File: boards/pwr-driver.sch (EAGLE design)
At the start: 24 parts

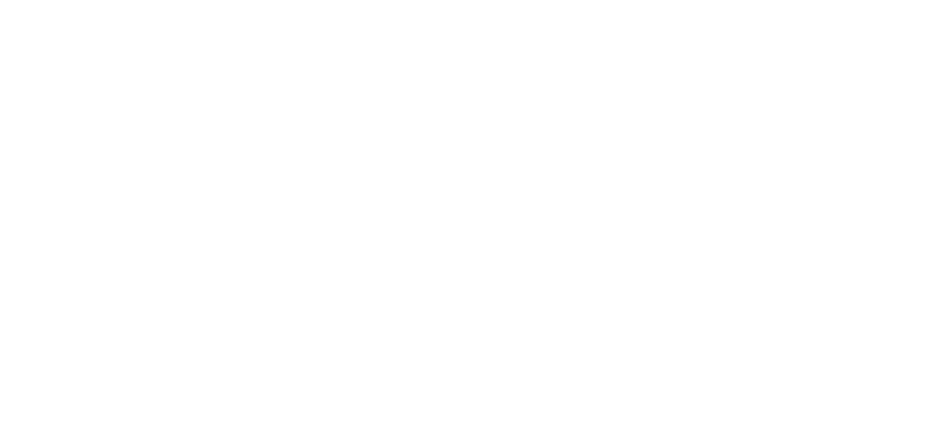
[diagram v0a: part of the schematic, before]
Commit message: dding start of parts lib for breakout board.
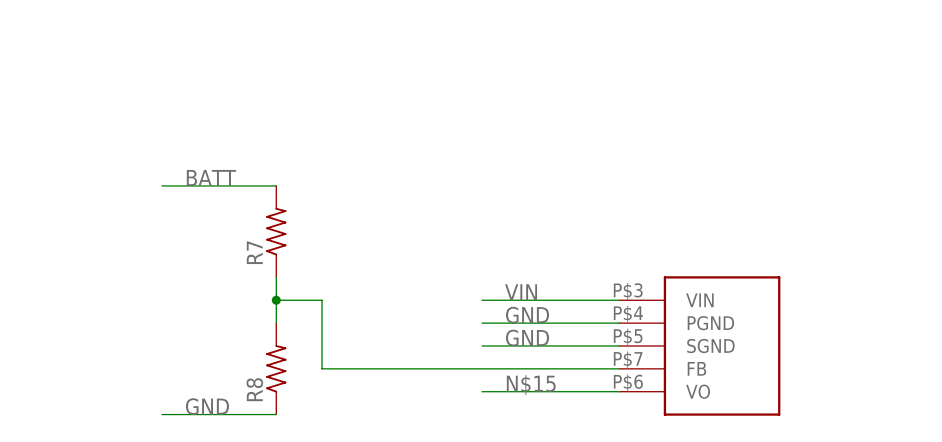
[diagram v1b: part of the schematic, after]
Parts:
- added R7, R8: (no value), resistor:R-US_R0603
- added U$1: MPM80, needed-parts:MPM80
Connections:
- new net BATT: R7.2
- new net N$15: U$1.VO
- new net N$4: R7.1, R8.2, U$1.FB
- net GND: now also R8.1, U$1.PGND, U$1.SGND
- net VIN: now also U$1.VIN
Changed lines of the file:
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@@
 <part name="R6" library="resistor" deviceset="R-US_" device="R0603" value="10k"/>
 <part name="C5" library="resistor" deviceset="C-US" device="C0603" value=".1uf"/>
+<part name="U$1" library="needed-parts" deviceset="MPM80" device=""/>
+<part name="R7" library="resistor" deviceset="R-US_" device="R0603"/>
+<part name="R8" library="resistor" deviceset="R-US_" device="R0603"/>
 </parts>
 <sheets>
@@
 <instance part="R6" gate="G$1" x="-66.04" y="20.32"/>
 <instance part="C5" gate="G$1" x="-68.58" y="15.24" rot="R90"/>
+<instance part="U$1" gate="G$1" x="96.52" y="-38.1"/>
+<instance part="R7" gate="G$1" x="48.26" y="-20.32" rot="R90"/>
+<instance part="R8" gate="G$1" x="48.26" y="-35.56" rot="R90"/>
 </instances>
 <busses>
@@
 <junction x="-71.12" y="15.24"/>
 </segment>
+<segment>
+<pinref part="R8" gate="G$1" pin="1"/>
+<wire x1="48.26" y1="-40.64" x2="35.56" y2="-40.64" width="0.1524" layer="91"/>
+<label x="38.1" y="-40.64" size="1.778" layer="95"/>
+</segment>
+<segment>
+<pinref part="U$1" gate="G$1" pin="PGND"/>
+<wire x1="86.36" y1="-30.48" x2="71.12" y2="-30.48" width="0.1524" layer="91"/>
+<label x="73.66" y="-30.48" size="1.778" layer="95"/>
+</segment>
+<segment>
+<pinref part="U$1" gate="G$1" pin="SGND"/>
+<wire x1="86.36" y1="-33.02" x2="71.12" y2="-33.02" width="0.1524" layer="91"/>
+<label x="73.66" y="-33.02" size="1.778" layer="95"/>
+</segment>
 </net>
 <net name="3V3" class="0">
@@
 <wire x1="154.94" y1="157.48" x2="127" y2="157.48" width="0.1524" layer="91"/>
 <label x="129.54" y="157.48" size="1.778" layer="95"/>
+</segment>
+<segment>
+<pinref part="U$1" gate="G$1" pin="VIN"/>
+<wire x1="86.36" y1="-27.94" x2="71.12" y2="-27.94" width="0.1524" layer="91"/>
+<label x="73.66" y="-27.94" size="1.778" layer="95"/>
 </segment>
 </net>
@@
 </segment>
 </net>
+<net name="N$4" class="0">
+<segment>
+<pinref part="R7" gate="G$1" pin="1"/>
+<pinref part="R8" gate="G$1" pin="2"/>
+<wire x1="48.26" y1="-25.4" x2="48.26" y2="-27.94" width="0.1524" layer="91"/>
+<pinref part="U$1" gate="G$1" pin="FB"/>
+<wire x1="48.26" y1="-27.94" x2="48.26" y2="-30.48" width="0.1524" layer="91"/>
+<wire x1="86.36" y1="-35.56" x2="53.34" y2="-35.56" width="0.1524" layer="91"/>
+<wire x1="53.34" y1="-35.56" x2="53.34" y2="-27.94" width="0.1524" layer="91"/>
+<wire x1="53.34" y1="-27.94" x2="48.26" y2="-27.94" width="0.1524" layer="91"/>
+<junction x="48.26" y="-27.94"/>
+</segment>
+</net>
+<net name="N$15" class="0">
+<segment>
+<pinref part="U$1" gate="G$1" pin="VO"/>
+<wire x1="86.36" y1="-38.1" x2="71.12" y2="-38.1" width="0.1524" layer="91"/>
+<label x="73.66" y="-38.1" size="1.778" layer="95"/>
+</segment>
+</net>
+<net name="BATT" class="0">
+<segment>
+<pinref part="R7" gate="G$1" pin="2"/>
+<wire x1="48.26" y1="-15.24" x2="35.56" y2="-15.24" width="0.1524" layer="91"/>
+<label x="38.1" y="-15.24" size="1.778" layer="95"/>
+</segment>
+</net>

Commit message: Added more parts and a readme.
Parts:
- removed IC1: (no value), v-reg:78XXS
- removed JP1: (no value), pinhead:PINHD-1X6
- removed R5: 10k, resistor:R-US_R0603
- removed U$10: NPN-T-SMALL, mgregg:NPN-T-SMALL
- removed U$7: OKR-T-W12-DC-TO-DC, mgregg:OKR-T-W12-DC-TO-DC
- added BATT: (no value), pinhead:PINHD-1X2
- added U$3: STEP-UP-FROM-AMAZON, needed-parts:STEP-UP-FROM-AMAZON
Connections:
- removed net N$15: U$1.VO
- removed net N$8: U$7.REMOTE-ON-OFF
- removed net SCREEN1: U$10.C
- net 3V3: no longer JP1.2
- net 5V: now also U$3.OUT+; no longer IC1.OUT, U$7.VOUT
- net BATT: now also BATT.1, U$1.VO, U$3.IN+
- net GND: now also BATT.2, U$3.IN-, U$3.OUT-; no longer IC1.GND, JP1.1, R5.1, U$10.E, U$7.GND
- net GPIO25: no longer JP1.4
- net SCL: no longer JP1.6
- net SCREEN: no longer R5.2, U$10.B
- net SDA: no longer JP1.5
- net TRIM: no longer U$7.TRIM
- net VIN: no longer IC1.IN, JP1.3, U$7.VIN
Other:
- note removed: "7805"

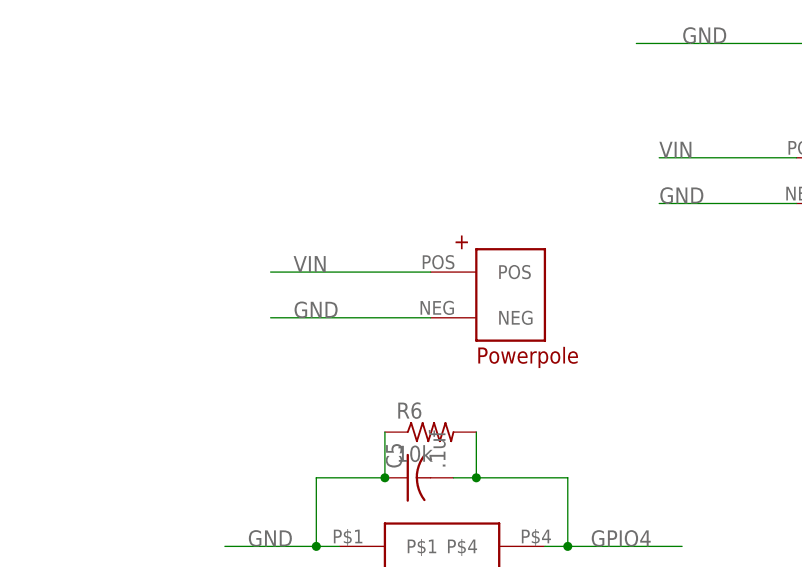
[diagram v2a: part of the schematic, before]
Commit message: Converted to three pin powerpole.
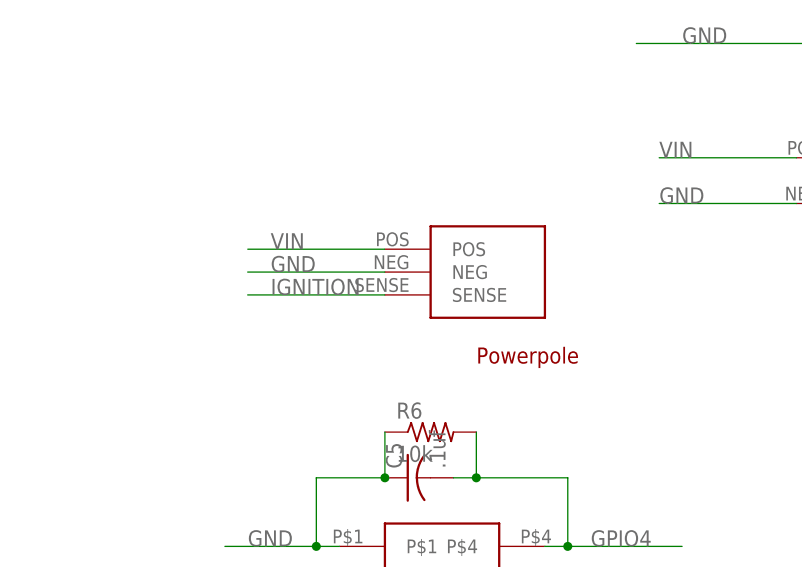
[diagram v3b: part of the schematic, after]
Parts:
- removed U$8: ANDERSON-DUAL, mgregg:ANDERSON-DUAL
- added U$7: POWERPOLE-WITH-SENSE, needed-parts:POWERPOLE-WITH-SENSE
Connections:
- new net IGNITION: U$7.SENSE
- net GND: now also U$7.NEG; no longer U$8.NEG
- net VIN: now also U$7.POS; no longer U$8.POS
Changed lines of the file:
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@@
 <?xml version="1.0" encoding="utf-8"?>
 <!DOCTYPE eagle SYSTEM "eagle.dtd">
-<eagle version="7.1.0">
+<eagle version="7.2.0">
 <drawing>
 <settings>
@@
 <layer number="111" name="tGTest" color="7" fill="1" visible="no" active="yes"/>
 <layer number="112" name="bGTest" color="7" fill="1" visible="no" active="yes"/>
+<layer number="113" name="IDFDebug" color="7" fill="1" visible="yes" active="yes"/>
 <layer number="116" name="Patch_BOT" color="9" fill="4" visible="no" active="yes"/>
 <layer number="117" name="mPads" color="7" fill="1" visible="no" active="yes"/>
@@
 <part name="U$6" library="mgregg" deviceset="AB26T-CRYSTAL" device=""/>
 <part name="C1" library="resistor" deviceset="C-US" device="C0805K"/>
-<part name="U$8" library="mgregg" deviceset="ANDERSON-DUAL" device=""/>
 <part name="R1" library="resistor" deviceset="R-US_" device="R0603" value="270"/>
 <part name="R2" library="resistor" deviceset="R-US_" device="R0603" value="43k"/>
@@
 <part name="U$3" library="needed-parts" deviceset="STEP-UP-FROM-AMAZON" device=""/>
 <part name="BATT" library="pinhead" deviceset="PINHD-1X2" device=""/>
+<part name="U$7" library="needed-parts" deviceset="POWERPOLE-WITH-SENSE" device=""/>
 </parts>
 <sheets>
@@
 <instance part="U$6" gate="G$1" x="-43.18" y="167.64"/>
 <instance part="C1" gate="G$1" x="-10.16" y="165.1"/>
-<instance part="U$8" gate="G$1" x="-58.42" y="38.1"/>
 <instance part="R1" gate="G$1" x="48.26" y="193.04"/>
 <instance part="R2" gate="G$1" x="48.26" y="185.42"/>
@@
 <instance part="U$3" gate="G$1" x="60.96" y="33.02"/>
 <instance part="BATT" gate="G$1" x="-45.72" y="91.44"/>
+<instance part="U$7" gate="G$1" x="-63.5" y="38.1"/>
 </instances>
 <busses>
@@
 <pinref part="C1" gate="G$1" pin="1"/>
 <wire x1="-10.16" y1="167.64" x2="-10.16" y2="170.18" width="0.1524" layer="91"/>
-</segment>
-<segment>
-<pinref part="U$8" gate="G$1" pin="NEG"/>
-<wire x1="-66.04" y1="33.02" x2="-83.82" y2="33.02" width="0.1524" layer="91"/>
-<label x="-81.28" y="33.02" size="1.778" layer="95"/>
 </segment>
 <segment>
@@
 <label x="-66.04" y="91.44" size="1.778" layer="95"/>
 </segment>
+<segment>
+<pinref part="U$7" gate="G$1" pin="NEG"/>
+<wire x1="-71.12" y1="38.1" x2="-86.36" y2="38.1" width="0.1524" layer="91"/>
+<label x="-83.82" y="38.1" size="1.778" layer="95"/>
+</segment>
 </net>
 <net name="3V3" class="0">
@@
 <net name="VIN" class="0">
 <segment>
-<pinref part="U$8" gate="G$1" pin="POS"/>
-<wire x1="-66.04" y1="38.1" x2="-83.82" y2="38.1" width="0.1524" layer="91"/>
-<label x="-81.28" y="38.1" size="1.778" layer="95"/>
-</segment>
-<segment>
 <pinref part="U$11" gate="G$1" pin="POS"/>
 <wire x1="-25.4" y1="50.8" x2="-40.64" y2="50.8" width="0.1524" layer="91"/>
@@
 <wire x1="86.36" y1="-27.94" x2="71.12" y2="-27.94" width="0.1524" layer="91"/>
 <label x="73.66" y="-27.94" size="1.778" layer="95"/>
+</segment>
+<segment>
+<pinref part="U$7" gate="G$1" pin="POS"/>
+<wire x1="-71.12" y1="40.64" x2="-86.36" y2="40.64" width="0.1524" layer="91"/>
+<label x="-83.82" y="40.64" size="1.778" layer="95"/>
 </segment>
 </net>
@@
 </segment>
 </net>
+<net name="IGNITION" class="0">
+<segment>
+<pinref part="U$7" gate="G$1" pin="SENSE"/>
+<wire x1="-71.12" y1="35.56" x2="-86.36" y2="35.56" width="0.1524" layer="91"/>
+<label x="-83.82" y="35.56" size="1.778" layer="95"/>
+</segment>
+</net>

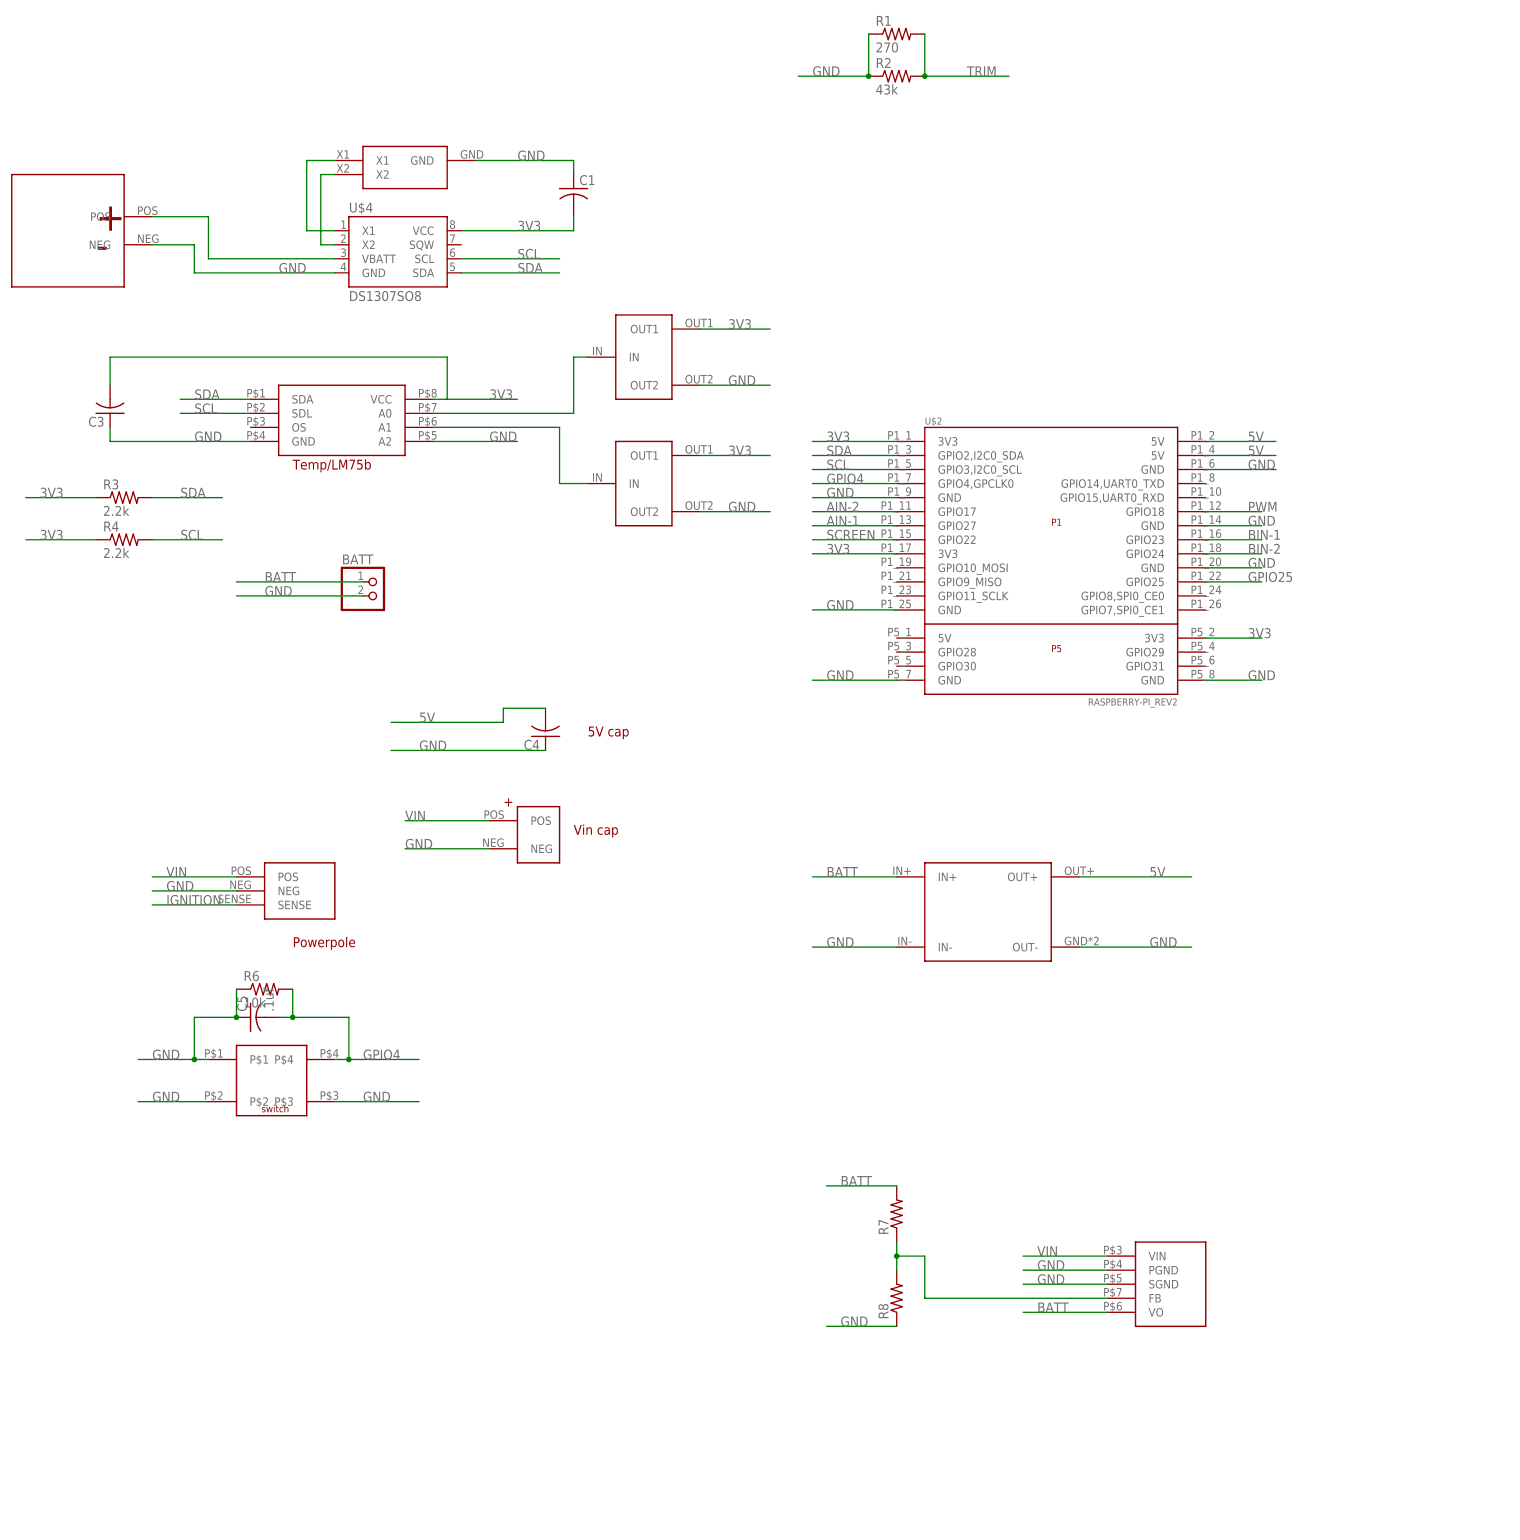
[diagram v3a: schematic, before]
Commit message: Adding Version 1.0 boards with the submitted gerbers.
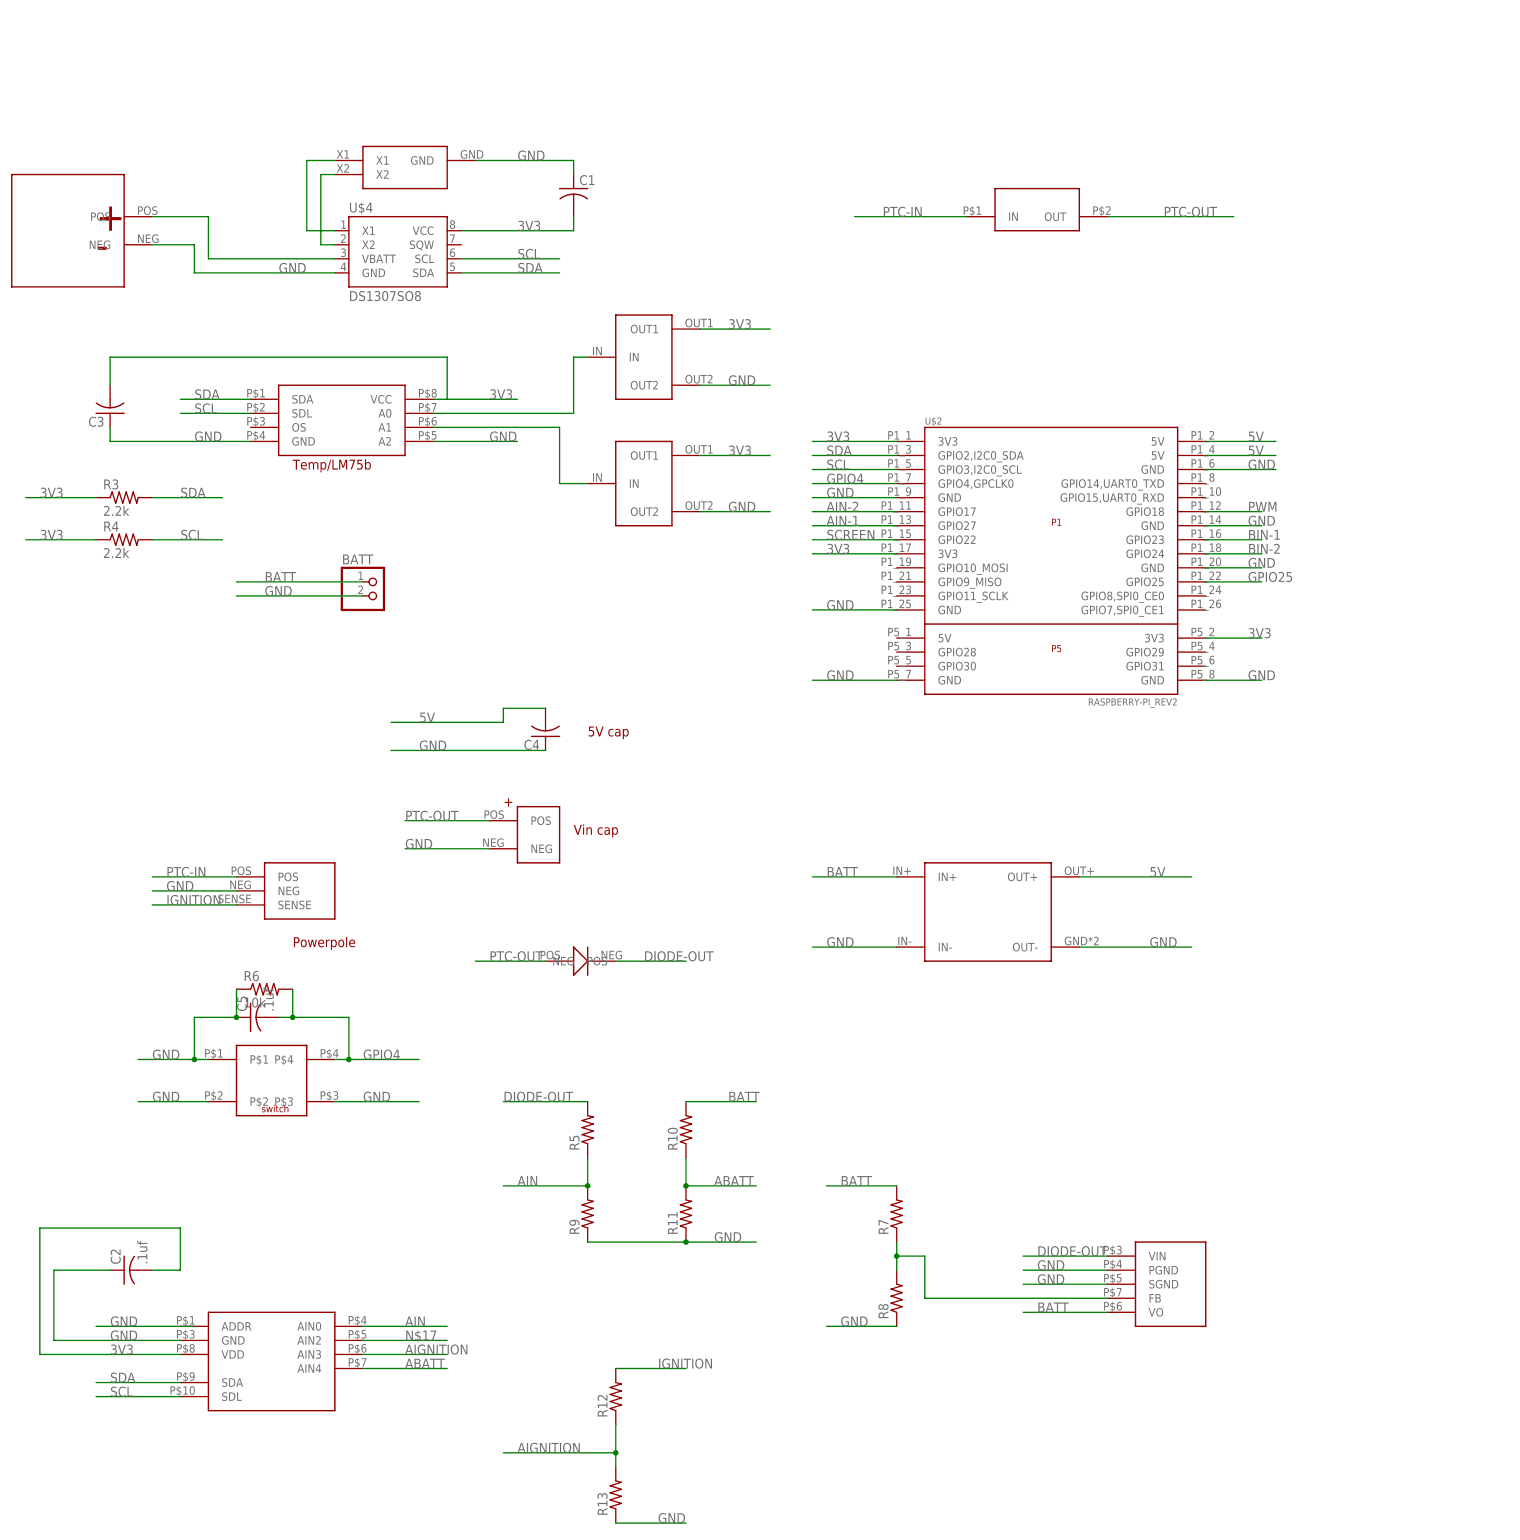
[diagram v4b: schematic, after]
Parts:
- removed R1: 270, resistor:R-US_R0603
- removed R2: 43k, resistor:R-US_R0603
- added C2: .1uf, resistor:C-USC0603
- added R10, R11, R12, R13, R5, R9: (no value), resistor:R-US_R0603
- added U$10: ADS1013, needed-parts:ADS1013
- added U$15: DIODE-403, needed-parts:DIODE-403
- added U$8: PTC, needed-parts:PTC
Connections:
- removed net TRIM: R1.2, R2.2
- removed net VIN: U$1.VIN, U$11.POS, U$7.POS
- new net ABATT: R10.1, R11.2, U$10.AIN4
- new net AIGNITION: R12.1, R13.2, U$10.AIN3
- new net AIN: R5.1, R9.2, U$10.AIN0
- new net DIODE-OUT: R5.2, U$1.VIN, U$15.NEG
- new net N$17: U$10.AIN2
- new net PTC-IN: U$7.POS, U$8.IN
- new net PTC-OUT: U$11.POS, U$15.POS, U$8.OUT
- net 3V3: now also C2.2, U$10.VDD
- net BATT: now also R10.2
- net GND: now also C2.1, R11.1, R13.1, R9.1, U$10.GND; no longer R1.1, R2.1
- net IGNITION: now also R12.2
- net SCL: now also U$10.SDL
- net SDA: now also U$10.SDA
